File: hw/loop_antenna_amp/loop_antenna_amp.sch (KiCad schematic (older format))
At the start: 73 parts, among them J1 ANT1, J2 ANT2, J3 GND, J4 Coax (solder), J5 Coax (SMA), Q1 MMBT3904, Q2 MMBT3904, Q3 MMBT3904, Q4 MMBT3904, Q5 PZT3904, Q6 PZT3904, T1 Isolation trafo, T2 Normalization trafo, T3 Output balun, U1 L78L10, U2 TL072

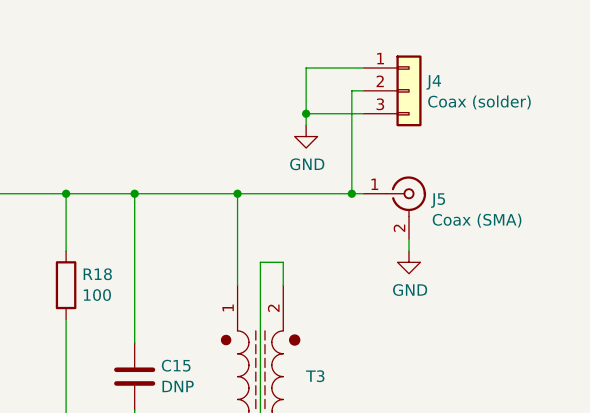
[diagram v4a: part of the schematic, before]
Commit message: Loop antenna: leave only SMA connector (coax can be soldered there)
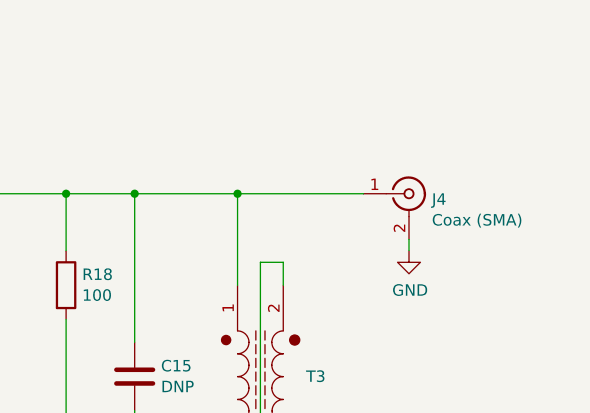
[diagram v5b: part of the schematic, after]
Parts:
- removed J4: Coax (solder), symbol Connector_Generic:Conn_01x03
- renumbered J5 to J4
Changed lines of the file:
@@
 	10500 1600 10500 1650
 $Comp
-L power:GND #PWR033
+L power:GND #PWR032
 U 1 1 60DDA9B5
 P 10500 1650
-F 0 "#PWR033" H 10500 1400 50  0001 C CNN
+F 0 "#PWR032" H 10500 1400 50  0001 C CNN
 F 1 "GND" H 10505 1477 50  0000 C CNN
 F 2 "" H 10500 1650 50  0001 C CNN
@@
 Connection ~ 9750 1400
 $Comp
-L Connector:Conn_Coaxial J5
+L Connector:Conn_Coaxial J4
 U 1 1 60DD6FDB
 P 10500 1400
-F 0 "J5" H 10600 1375 50  0000 L CNN
+F 0 "J4" H 10600 1375 50  0000 L CNN
 F 1 "Coax (SMA)" H 10600 1284 50  0000 L CNN
 F 2 "Connector_Coaxial:SMA_Amphenol_132134_Vertical" H 10500 1400 50  0001 C CNN
@@
 Connection ~ 5000 6650
 Wire Wire Line
-	10300 1400 10250 1400
-$Comp
-L Connector_Generic:Conn_01x03 J4
-U 1 1 6174AD77
-P 10500 950
-F 0 "J4" H 10580 992 50  0000 L CNN
-F 1 "Coax (solder)" H 10580 901 50  0000 L CNN
-F 2 "" H 10500 950 50  0001 C CNN
-F 3 "~" H 10500 950 50  0001 C CNN
-	1    10500 950
-	1    0    0    -1
-$EndComp
-$Comp
-L power:GND #PWR031
-U 1 1 6175A2AC
-P 10050 1100
-F 0 "#PWR031" H 10050 850 50  0001 C CNN
-F 1 "GND" H 10055 927 50  0000 C CNN
-F 2 "" H 10050 1100 50  0001 C CNN
-F 3 "" H 10050 1100 50  0001 C CNN
-	1    10050 1100
-	1    0    0    -1
-$EndComp
-Wire Wire Line
 	7900 5650 7700 5650
 Wire Wire Line
@@
 $EndComp
 $Comp
-L power:GND #PWR032
+L power:GND #PWR031
 U 1 1 617D06AB
 P 10350 4000
-F 0 "#PWR032" H 10350 3750 50  0001 C CNN
+F 0 "#PWR031" H 10350 3750 50  0001 C CNN
 F 1 "GND" H 10355 3827 50  0000 C CNN
 F 2 "" H 10350 4000 50  0001 C CNN
@@
 Wire Wire Line
 	5250 1750 5400 1750
-Connection ~ 10250 1400
-Wire Wire Line
-	10250 1400 9750 1400
-Wire Wire Line
-	10300 950  10250 950
-Wire Wire Line
-	10250 950  10250 1400
-Wire Wire Line
-	10300 1050 10050 1050
-Wire Wire Line
-	10050 1050 10050 1100
-Wire Wire Line
-	10300 850  10050 850
-Wire Wire Line
-	10050 850  10050 1050
-Connection ~ 10050 1050
 Wire Wire Line
 	5250 2650 5400 2650
@@
 Wire Wire Line
 	4050 6650 4500 6650
+Wire Wire Line
+	9750 1400 10300 1400
 $EndSCHEMATC

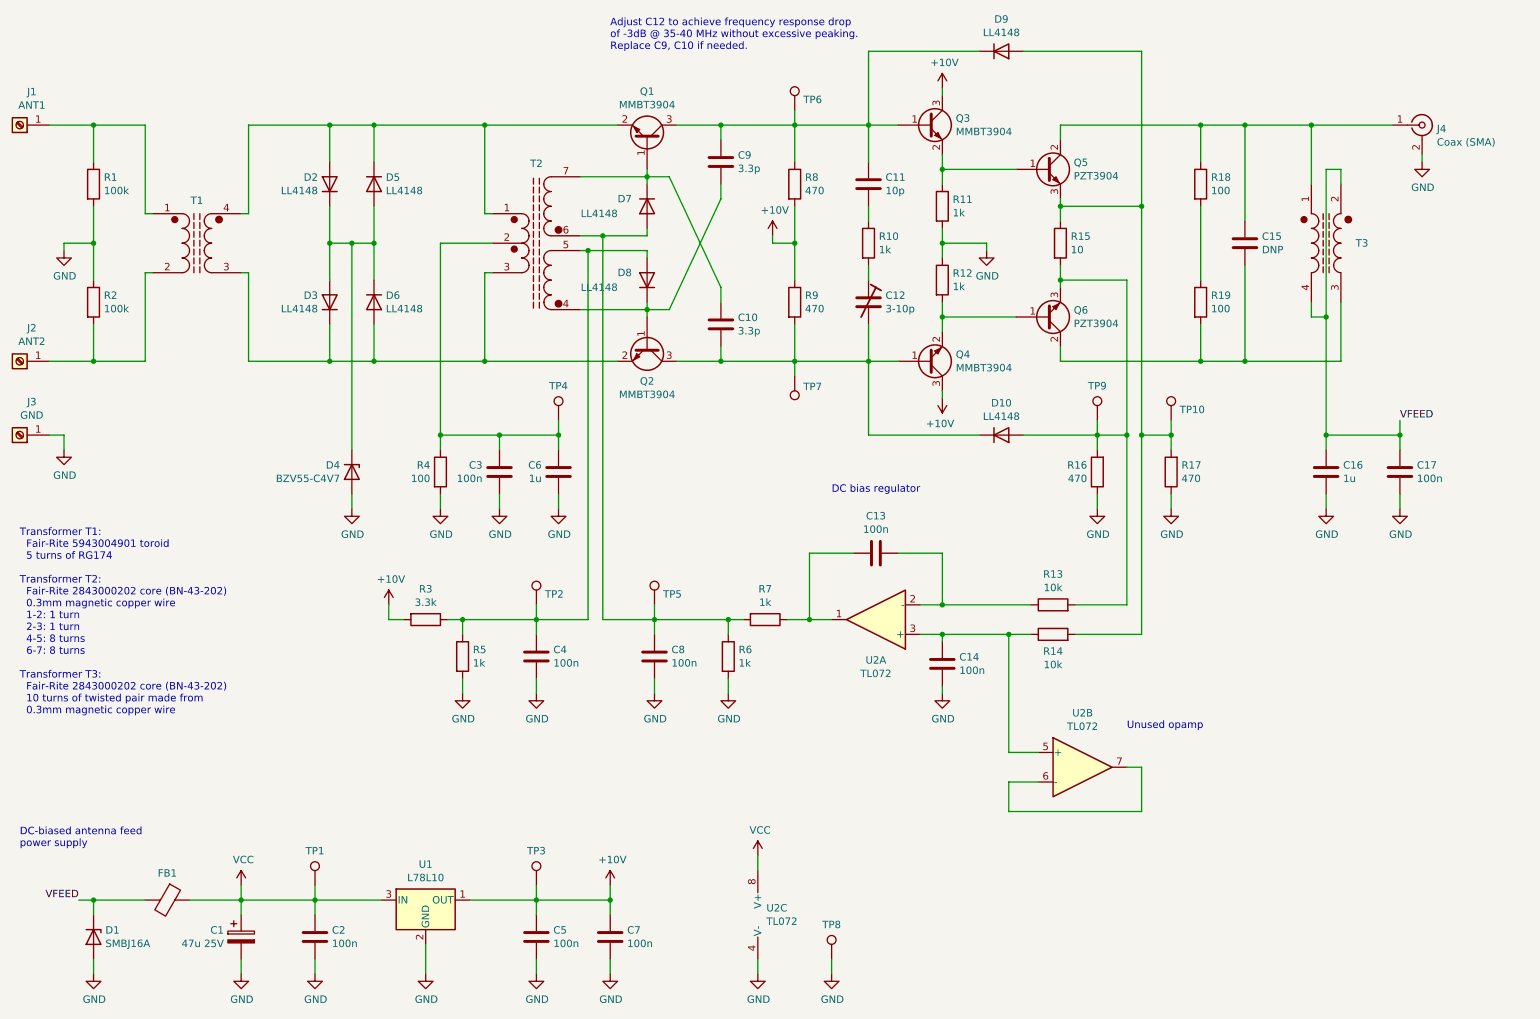
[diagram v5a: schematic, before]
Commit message: Loop antenna: PCB layout almost completed
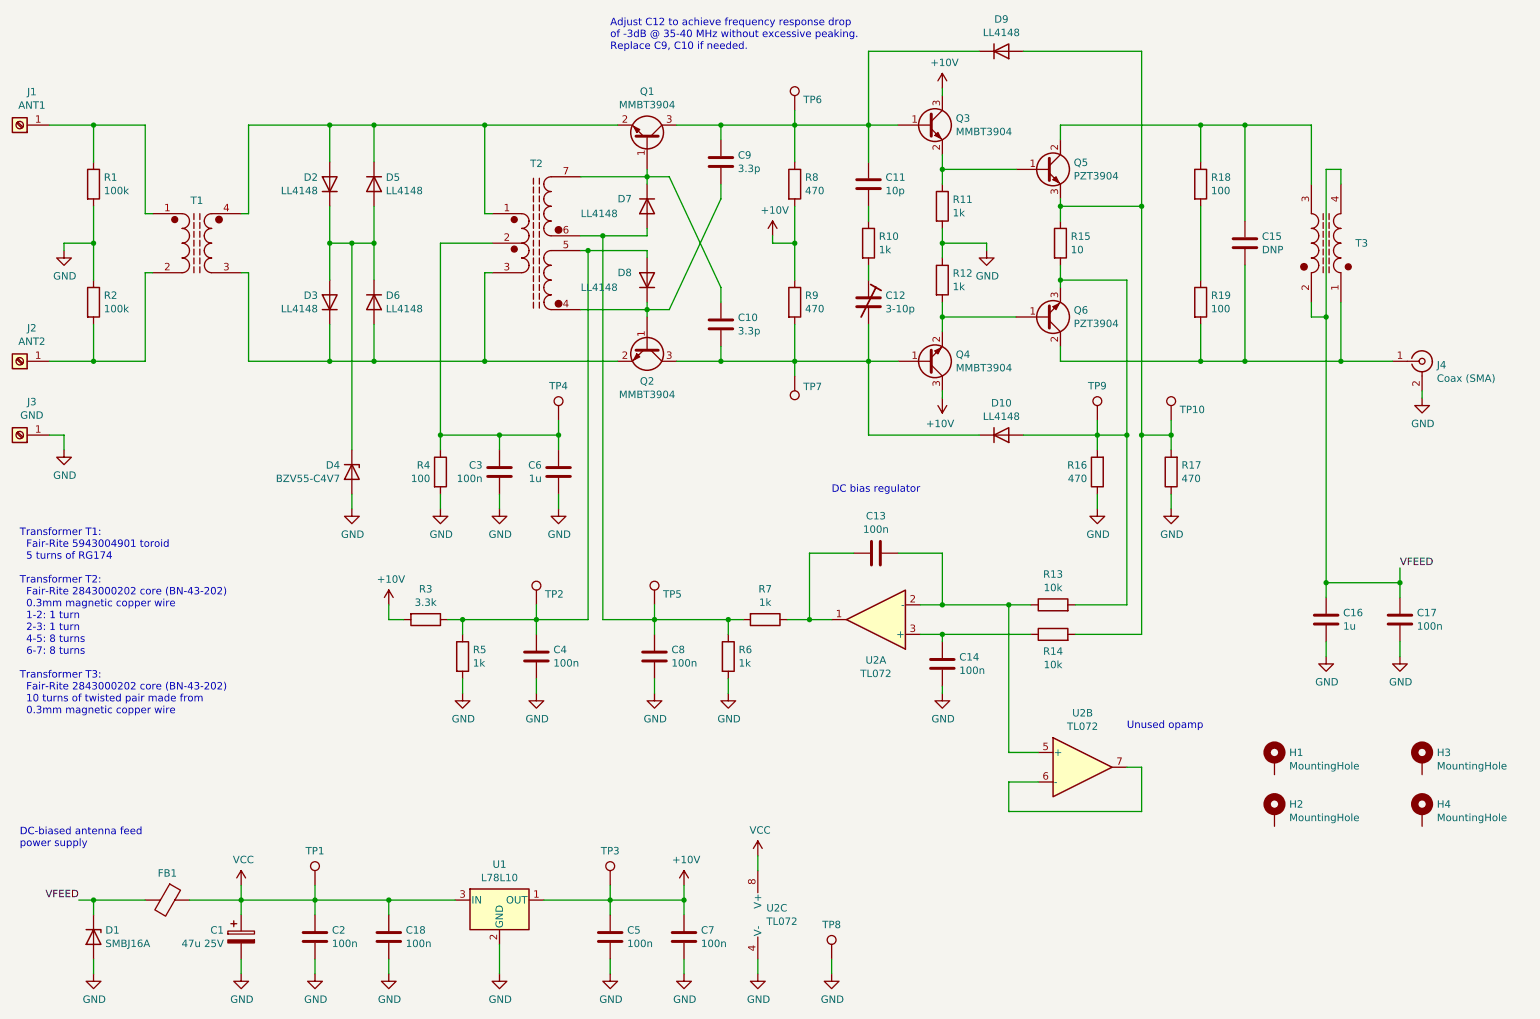
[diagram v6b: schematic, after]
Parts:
- added C18: 100n, Capacitor_SMD:C_0805_2012Metric_Pad1.15x1.40mm_HandSolder, symbol Device:C
- added H1, H2, H3, H4: MountingHole, local_footprints:MountingHole, symbol Mechanical:MountingHole_Pad
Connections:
- net GND: now also C18.2
- net VCC: now also C18.1
- net at C15.1, Q5.2 (C), Q5.4 (C)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: now also T3.3 (BB); no longer J4.1 (In), T3.1 (AA)
- net at C15.2, Q6.2 (C), Q6.4 (C)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: now also J4.1 (In), T3.1 (AA); no longer T3.3 (BB)
- net at C13.1, R13.1, U2.2 (-): now also U2.5 (+)
- net at C14.1, R14.1, U2.3 (+): no longer U2.5 (+)
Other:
- moved on the sheet: C16, C17, C5, C7, J4, TP3, U1

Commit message: Loop antenna: modify DC servo feedback to allow 0 ohm degeneration in output stage
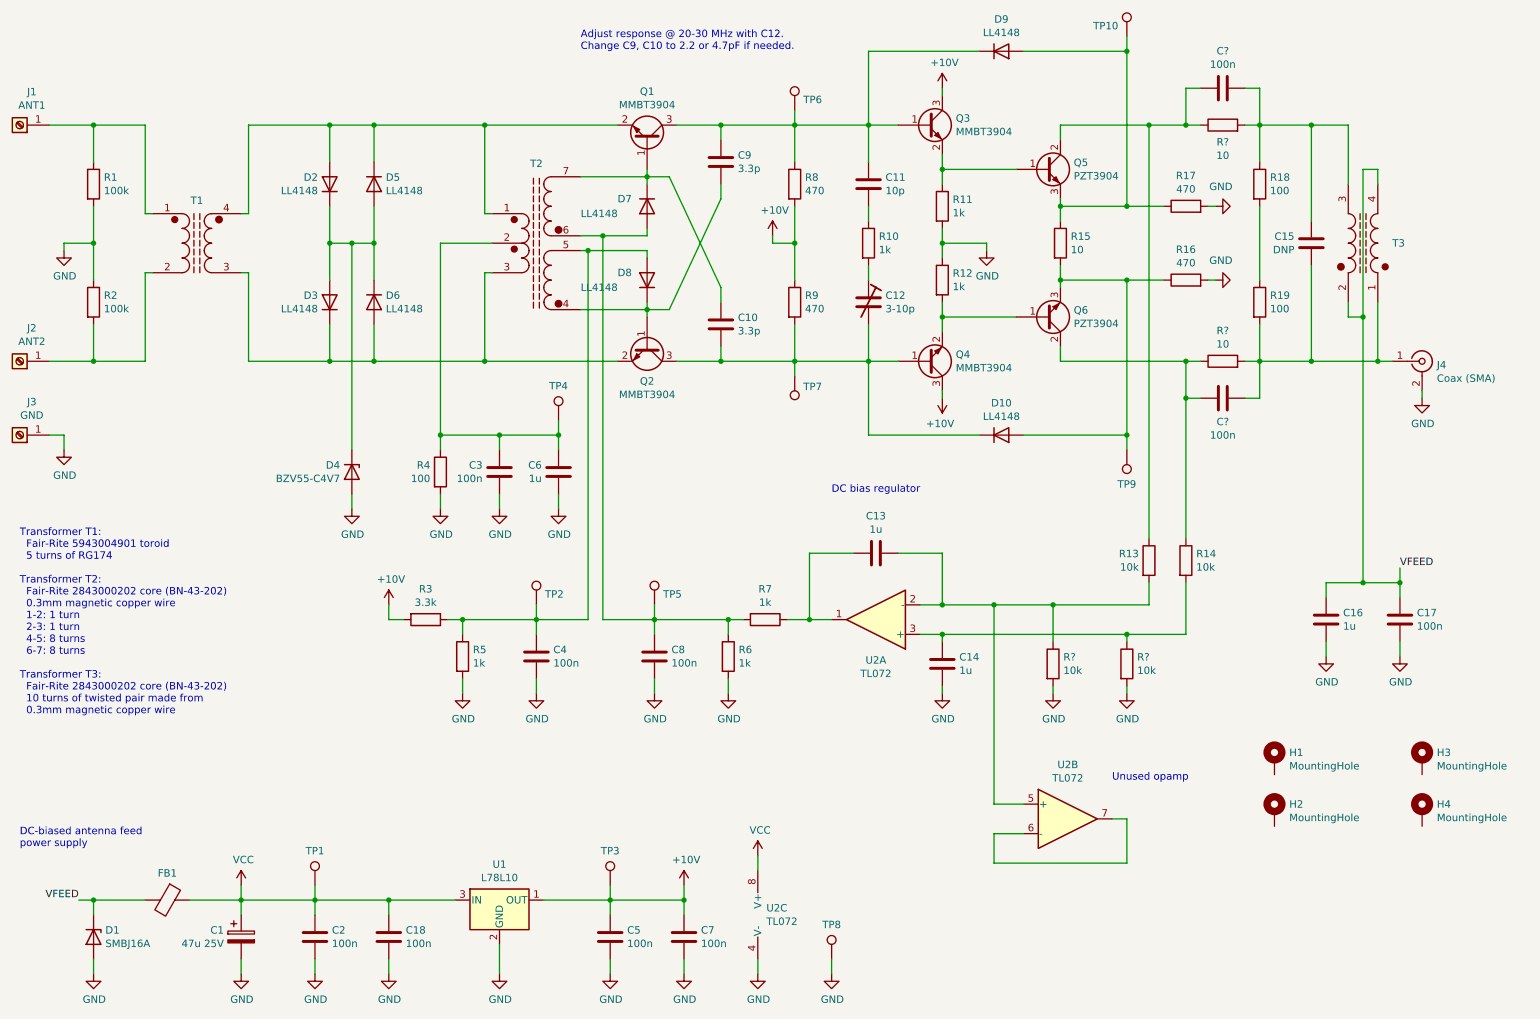
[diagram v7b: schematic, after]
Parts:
- added C? (x2): 100n, Capacitor_SMD:C_0805_2012Metric_Pad1.15x1.40mm_HandSolder, symbol Device:C
- added R? (x2): 10, Resistor_SMD:R_0805_2012Metric_Pad1.15x1.40mm_HandSolder, symbol Device:R
- added R? (x2): 10k, Resistor_SMD:R_0805_2012Metric_Pad1.15x1.40mm_HandSolder, symbol Device:R
- C13, C14: value 100n -> 1u; footprint Capacitor_THT:C_Rect_L7.0mm_W2.5mm_P5.00mm -> Capacitor_THT:C_Rect_L7.0mm_W4.5mm_P5.00mm
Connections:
- net GND: now also R16.2, R17.2, R?.2, R?.2; no longer R16.1, R17.1
- net at C15.1, R18.1, T3.3 (BB): now also C?.1, R?.2; no longer Q5.2 (C), Q5.4 (C)
- net at D9.2 (A), Q5.3 (E), R15.1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: now also R17.1; no longer R14.2, R17.2
- net at C15.2, J4.1 (In), R19.2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: now also C?.1, R?.2; no longer Q6.2 (C), Q6.4 (C)
- net at D10.2 (A), Q6.3 (E), R15.2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: now also R16.1; no longer R13.2, R16.2
- net at C13.1, U2.2 (-), U2.5 (+): now also R13.2, R?.1; no longer R13.1
- net at C14.1, U2.3 (+): now also R14.2, R?.1; no longer R14.1
- new net: C?.2, Q5.2 (C), Q5.4 (C), R13.1, R?.1
- new net: C?.2, Q6.2 (C), Q6.4 (C), R14.1, R?.1
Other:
- note added: "Adjust response @ 20-30 MHz with C12.\nChange C9, C10 to 2.2 or 4.7pF if needed."
- note removed: "Adjust C12 to achieve frequency response drop\nof -3dB @ 35-40 MHz without excessive peaking.\nReplace C9, C10 if needed."
- moved on the sheet: C15, R13, R14, R16, R17, R18, R19, T3, TP10, TP9, U2B

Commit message: Loop antenna amp: remove DC bias from output balun (bias current was too high)
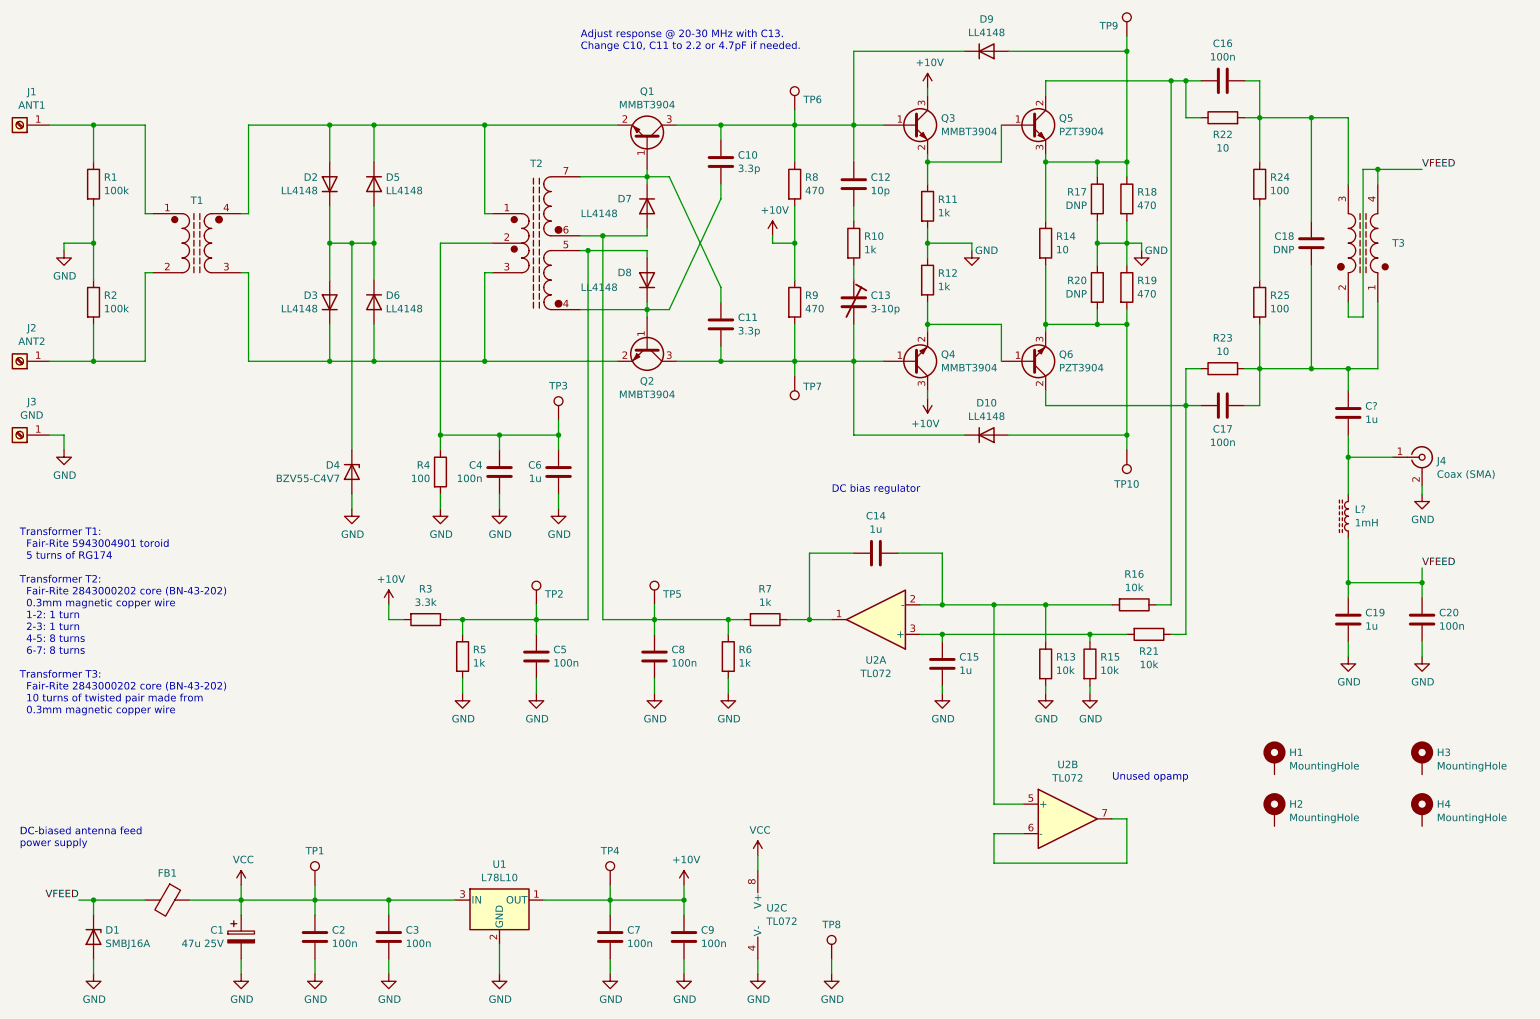
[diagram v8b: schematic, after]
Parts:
- added C?: 1u, Capacitor_THT:C_Rect_L7.2mm_W5.5mm_P5.00mm_FKS2_FKP2_MKS2_MKP2, symbol Device:C
- added L?: 1mH, Inductor_THT:L_Radial_D8.7mm_P5.00mm_Fastron_07HCP, symbol Device:L_Core_Ferrite
- added R17, R20: DNP, Resistor_SMD:R_0805_2012Metric_Pad1.15x1.40mm_HandSolder, symbol Device:R
- gave numbers to parts that had none: 6
- renumbered C9 to C10, C10 to C11, C11 to C12, C12 to C13, C13 to C14, C14 to C15, C15 to C18, C16 to C19, C17 to C20, C18 to C3, C3 to C4, C4 to C5, C5 to C7, C7 to C9, R15 to R14, R13 to R16, R17 to R18, R16 to R19, R14 to R21, R18 to R24, R19 to R25, TP9 to TP10, TP4 to TP3, TP3 to TP4, TP10 to TP9
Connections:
- net GND: now also R19.1, R17.2, R20.1; no longer R19.2
- net VFEED: now also L?.1
- net at D9.2 (A), Q5.3 (E), R14.1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: now also R17.1
- net at D10.2 (A), Q6.3 (E), R14.2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: now also R19.2, R20.2; no longer R19.1
- net at C17.1, C18.2, R23.2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: now also C?.2; no longer J4.1 (In)
- new net: C?.1, J4.1 (In), L?.2
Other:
- note added: "Adjust response @ 20-30 MHz with C13.\nChange C10, C11 to 2.2 or 4.7pF if needed."
- note removed: "Adjust response @ 20-30 MHz with C12.\nChange C9, C10 to 2.2 or 4.7pF if needed."
- moved on the sheet: C12, C13, C16, C17, C19, C20, D10, D9, J4, Q3, Q4, Q5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
